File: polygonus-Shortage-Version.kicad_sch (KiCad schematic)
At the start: 10 parts, among them J1 Conn_01x01, J2 Conn_01x01, J3 Conn_01x01, J4 Conn_01x32, J5 Conn_01x32, J6 Conn_01x16, J7 Conn_01x16

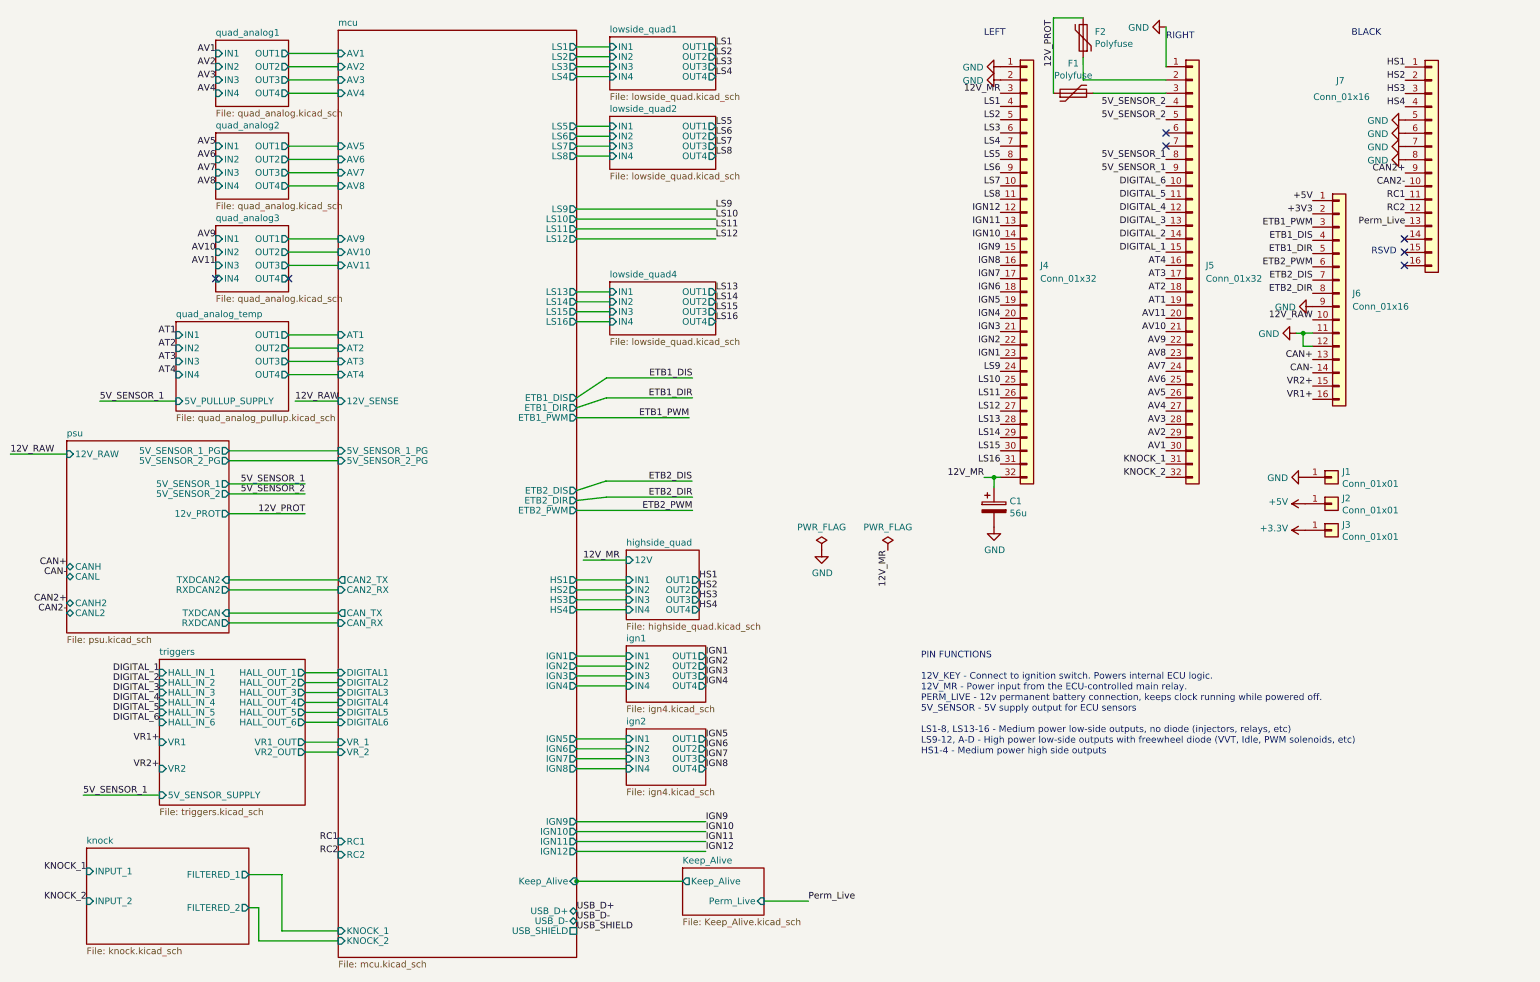
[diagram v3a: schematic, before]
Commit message: route trigger scope
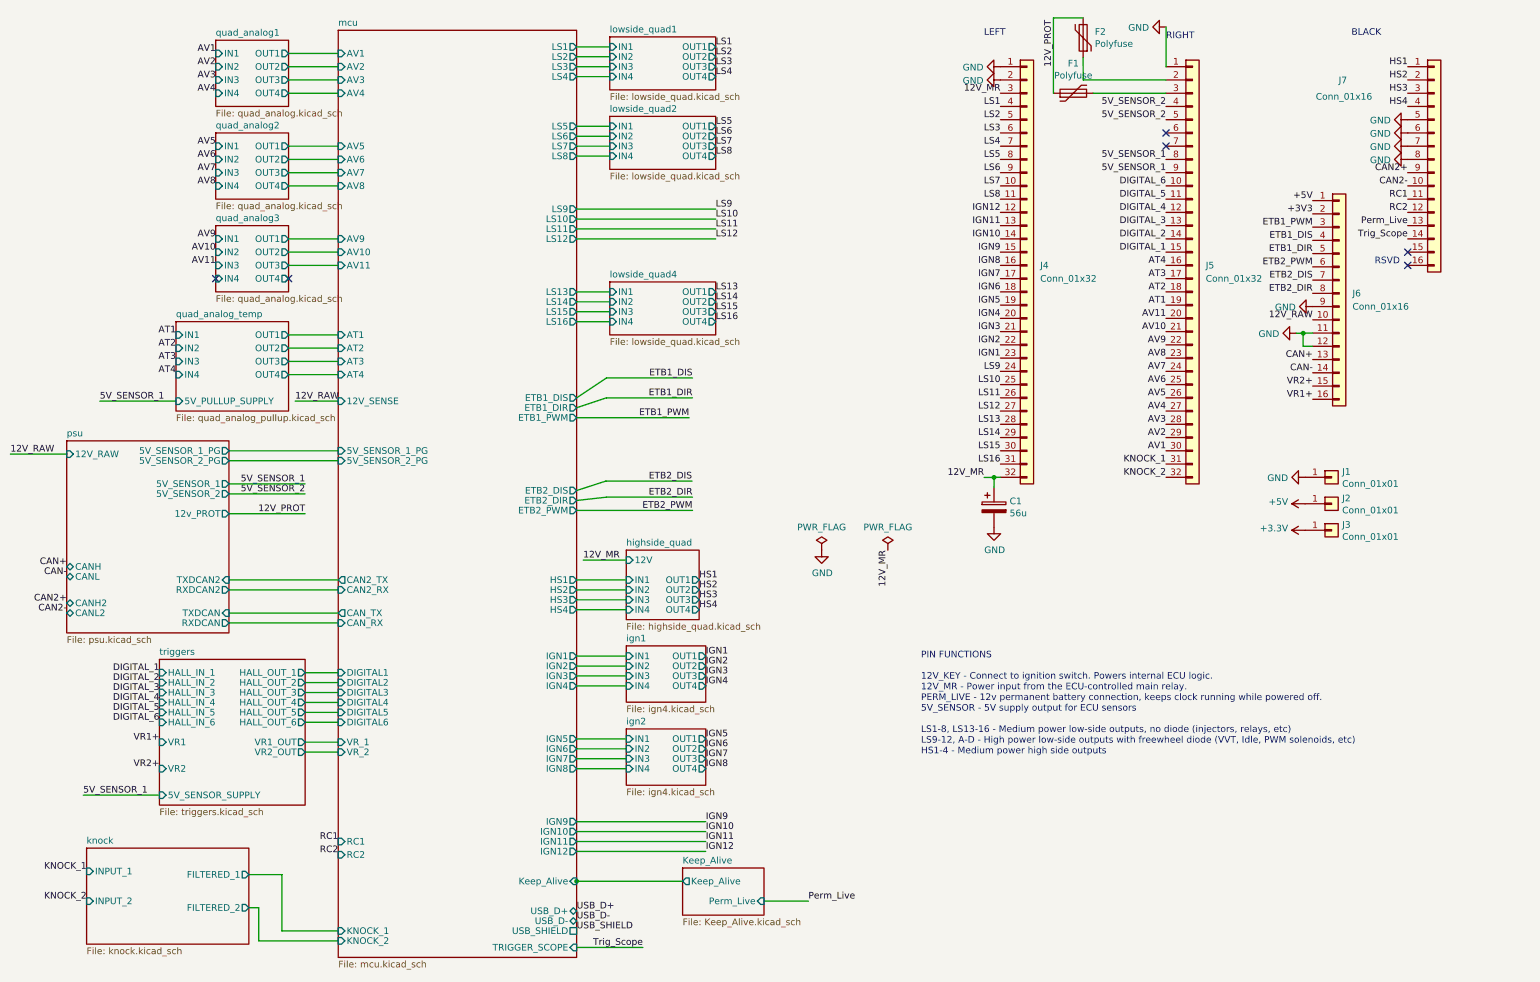
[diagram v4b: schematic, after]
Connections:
- net Trig_Scope: now reaches J7.14 (Pin_14)
- no-connect marks 7 -> 6
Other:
- sheet mcu ports: added TRIGGER_SCOPE; removed none
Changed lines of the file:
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@@
   )
   (no_connect (at 45.085 64.77))
+  (no_connect (at 273.685 59.69))
   (no_connect (at 59.055 64.77))
-  (no_connect (at 273.05 59.69))
   (no_connect (at 227.33 36.83))
   (no_connect (at 227.33 39.37))
-  (no_connect (at 273.05 62.23))
-  (no_connect (at 273.05 57.15))
+  (no_connect (at 273.685 62.23))
   (wire (pts (xy 62.23 144.145) (xy 68.58 144.145))
     (stroke (width 0) (type default))
@@
     (stroke (width 0) (type default))
   )
+  (wire (pts (xy 114.3 193.04) (xy 127 193.04))
+    (stroke (width 0) (type default))
+  )
   (wire (pts (xy 114.3 139.065) (xy 123.825 139.065))
     (stroke (width 0) (type default))
@@
     (effects (font (size 1.27 1.27)) (justify left bottom))
   )
-  (text "RSVD" (at 266.7 60.325 0)
+  (text "RSVD" (at 267.335 62.23 0)
     (effects (font (size 1.27 1.27)) (justify left bottom))
   )
@@
     (effects (font (size 1.27 1.27)) (justify right bottom))
   )
-  (label "HS1" (at 273.2114 24.1919 180) (fields_autoplaced)
-    (effects (font (size 1.27 1.27)) (justify right bottom))
-  )
-  (label "CAN2-" (at 273.2114 47.0519 180) (fields_autoplaced)
+  (label "HS1" (at 273.685 24.13 180) (fields_autoplaced)
+    (effects (font (size 1.27 1.27)) (justify right bottom))
+  )
+  (label "CAN2-" (at 273.685 46.99 180) (fields_autoplaced)
     (effects (font (size 1.27 1.27)) (justify right bottom))
   )
@@
     (effects (font (size 1.27 1.27)) (justify right bottom))
   )
+  (label "Trig_Scope" (at 273.685 57.15 180) (fields_autoplaced)
+    (effects (font (size 1.27 1.27)) (justify right bottom))
+  )
   (label "DIGITAL_3" (at 227.33 54.61 180) (fields_autoplaced)
     (effects (font (size 1.27 1.27)) (justify right bottom))
@@
     (effects (font (size 1.27 1.27)) (justify right bottom))
   )
-  (label "RC2" (at 273.2114 52.1319 180) (fields_autoplaced)
+  (label "RC2" (at 273.685 52.07 180) (fields_autoplaced)
     (effects (font (size 1.27 1.27)) (justify right bottom))
   )
@@
     (effects (font (size 1.27 1.27)) (justify right bottom))
   )
-  (label "HS3" (at 273.2114 29.2719 180) (fields_autoplaced)
+  (label "HS3" (at 273.685 29.21 180) (fields_autoplaced)
     (effects (font (size 1.27 1.27)) (justify right bottom))
   )
@@
     (effects (font (size 1.27 1.27)) (justify right bottom))
   )
-  (label "HS2" (at 273.2114 26.7319 180) (fields_autoplaced)
+  (label "HS2" (at 273.685 26.67 180) (fields_autoplaced)
     (effects (font (size 1.27 1.27)) (justify right bottom))
   )
@@
     (effects (font (size 1.27 1.27)) (justify left bottom))
   )
-  (label "Perm_Live" (at 273.2114 54.6719 180) (fields_autoplaced)
-    (effects (font (size 1.27 1.27)) (justify right bottom))
-  )
-  (label "RC1" (at 273.2114 49.5919 180) (fields_autoplaced)
+  (label "Perm_Live" (at 273.685 54.61 180) (fields_autoplaced)
+    (effects (font (size 1.27 1.27)) (justify right bottom))
+  )
+  (label "RC1" (at 273.685 49.53 180) (fields_autoplaced)
     (effects (font (size 1.27 1.27)) (justify right bottom))
   )
@@
     (effects (font (size 1.27 1.27)) (justify right bottom))
   )
+  (label "Trig_Scope" (at 127 193.04 180) (fields_autoplaced)
+    (effects (font (size 1.27 1.27)) (justify right bottom))
+  )
   (label "AT4" (at 227.33 62.23 180) (fields_autoplaced)
     (effects (font (size 1.27 1.27)) (justify right bottom))
@@
     (effects (font (size 1.27 1.27)) (justify right bottom))
   )
-  (label "CAN2+" (at 273.2114 44.5119 180) (fields_autoplaced)
+  (label "CAN2+" (at 273.685 44.45 180) (fields_autoplaced)
     (effects (font (size 1.27 1.27)) (justify right bottom))
   )
@@
     (effects (font (size 1.27 1.27)) (justify left bottom))
   )
-  (label "HS4" (at 273.2114 31.8119 180) (fields_autoplaced)
+  (label "HS4" (at 273.685 31.75 180) (fields_autoplaced)
     (effects (font (size 1.27 1.27)) (justify right bottom))
   )
@@
     )
   )
-  (symbol (lib_id "power:GND") (at 273.2114 39.4319 270) (unit 1)
-    (in_bom yes) (on_board yes) (dnp no)
-    (property "Reference" "#PWR013" (at 266.8614 39.4319 0)
-      (effects (font (size 1.27 1.27)) hide)
-    )
-    (property "Value" "GND" (at 269.9602 39.5589 90)
-      (effects (font (size 1.27 1.27)) (justify right))
-    )
-    (property "Footprint" "" (at 273.2114 39.4319 0)
-      (effects (font (size 1.27 1.27)) hide)
-    )
-    (property "Datasheet" "" (at 273.2114 39.4319 0)
+  (symbol (lib_id "power:GND") (at 273.685 39.37 270) (unit 1)
+    (in_bom yes) (on_board yes) (dnp no)
+    (property "Reference" "#PWR013" (at 267.335 39.37 0)
+      (effects (font (size 1.27 1.27)) hide)
+    )
+    (property "Value" "GND" (at 270.4338 39.497 90)
+      (effects (font (size 1.27 1.27)) (justify right))
+    )
+    (property "Footprint" "" (at 273.685 39.37 0)
+      (effects (font (size 1.27 1.27)) hide)
+    )
+    (property "Datasheet" "" (at 273.685 39.37 0)
       (effects (font (size 1.27 1.27)) hide)
     )
@@
     )
   )
-  (symbol (lib_id "power:GND") (at 273.2114 41.9719 270) (unit 1)
-    (in_bom yes) (on_board yes) (dnp no)
-    (property "Reference" "#PWR014" (at 266.8614 41.9719 0)
-      (effects (font (size 1.27 1.27)) hide)
-    )
-    (property "Value" "GND" (at 269.9602 42.0989 90)
-      (effects (font (size 1.27 1.27)) (justify right))
-    )
-    (property "Footprint" "" (at 273.2114 41.9719 0)
-      (effects (font (size 1.27 1.27)) hide)
-    )
-    (property "Datasheet" "" (at 273.2114 41.9719 0)
+  (symbol (lib_id "power:GND") (at 273.685 41.91 270) (unit 1)
+    (in_bom yes) (on_board yes) (dnp no)
+    (property "Reference" "#PWR014" (at 267.335 41.91 0)
+      (effects (font (size 1.27 1.27)) hide)
+    )
+    (property "Value" "GND" (at 270.4338 42.037 90)
+      (effects (font (size 1.27 1.27)) (justify right))
+    )
+    (property "Footprint" "" (at 273.685 41.91 0)
+      (effects (font (size 1.27 1.27)) hide)
+    )
+    (property "Datasheet" "" (at 273.685 41.91 0)
       (effects (font (size 1.27 1.27)) hide)
     )
@@
     )
   )
-  (symbol (lib_id "power:GND") (at 273.2114 34.3519 270) (unit 1)
-    (in_bom yes) (on_board yes) (dnp no)
-    (property "Reference" "#PWR011" (at 266.8614 34.3519 0)
-      (effects (font (size 1.27 1.27)) hide)
-    )
-    (property "Value" "GND" (at 269.9602 34.4789 90)
-      (effects (font (size 1.27 1.27)) (justify right))
-    )
-    (property "Footprint" "" (at 273.2114 34.3519 0)
-      (effects (font (size 1.27 1.27)) hide)
-    )
-    (property "Datasheet" "" (at 273.2114 34.3519 0)
+  (symbol (lib_id "power:GND") (at 273.685 34.29 270) (unit 1)
+    (in_bom yes) (on_board yes) (dnp no)
+    (property "Reference" "#PWR011" (at 267.335 34.29 0)
+      (effects (font (size 1.27 1.27)) hide)
+    )
+    (property "Value" "GND" (at 270.4338 34.417 90)
+      (effects (font (size 1.27 1.27)) (justify right))
+    )
+    (property "Footprint" "" (at 273.685 34.29 0)
+      (effects (font (size 1.27 1.27)) hide)
+    )
+    (property "Datasheet" "" (at 273.685 34.29 0)
       (effects (font (size 1.27 1.27)) hide)
     )
@@
     )
   )
-  (symbol (lib_id "power:GND") (at 273.2114 36.8919 270) (unit 1)
-    (in_bom yes) (on_board yes) (dnp no)
-    (property "Reference" "#PWR012" (at 266.8614 36.8919 0)
-      (effects (font (size 1.27 1.27)) hide)
-    )
-    (property "Value" "GND" (at 269.9602 37.0189 90)
-      (effects (font (size 1.27 1.27)) (justify right))
-    )
-    (property "Footprint" "" (at 273.2114 36.8919 0)
-      (effects (font (size 1.27 1.27)) hide)
-    )
-    (property "Datasheet" "" (at 273.2114 36.8919 0)
+  (symbol (lib_id "power:GND") (at 273.685 36.83 270) (unit 1)
+    (in_bom yes) (on_board yes) (dnp no)
+    (property "Reference" "#PWR012" (at 267.335 36.83 0)
+      (effects (font (size 1.27 1.27)) hide)
+    )
+    (property "Value" "GND" (at 270.4338 36.957 90)
+      (effects (font (size 1.27 1.27)) (justify right))
+    )
+    (property "Footprint" "" (at 273.685 36.83 0)
+      (effects (font (size 1.27 1.27)) hide)
+    )
+    (property "Datasheet" "" (at 273.685 36.83 0)
       (effects (font (size 1.27 1.27)) hide)
     )
@@
     )
   )
-  (symbol (lib_id "Connector_Generic:Conn_01x16") (at 278.2914 41.9719 0) (unit 1)
-    (in_bom yes) (on_board yes) (dnp no)
-    (property "Reference" "J7" (at 259.9581 26.7811 0)
-      (effects (font (size 1.27 1.27)) (justify left))
-    )
-    (property "Value" "Conn_01x16" (at 255.5749 29.9238 0)
-      (effects (font (size 1.27 1.27)) (justify left))
-    )
-    (property "Footprint" "Connector_PinHeader_2.54mm:PinHeader_1x16_P2.54mm_Vertical" (at 278.2914 41.9719 0)
-      (effects (font (size 1.27 1.27)) hide)
-    )
-    (property "Datasheet" "~" (at 278.2914 41.9719 0)
+  (symbol (lib_id "Connector_Generic:Conn_01x16") (at 278.765 41.91 0) (unit 1)
+    (in_bom yes) (on_board yes) (dnp no)
+    (property "Reference" "J7" (at 260.4317 26.7192 0)
+      (effects (font (size 1.27 1.27)) (justify left))
+    )
+    (property "Value" "Conn_01x16" (at 256.0485 29.8619 0)
+      (effects (font (size 1.27 1.27)) (justify left))
+    )
+    (property "Footprint" "Connector_PinHeader_2.54mm:PinHeader_1x16_P2.54mm_Vertical" (at 278.765 41.91 0)
+      (effects (font (size 1.27 1.27)) hide)
+    )
+    (property "Datasheet" "~" (at 278.765 41.91 0)
       (effects (font (size 1.27 1.27)) hide)
     )
@@
       (effects (font (size 1.27 1.27)) (justify left))
     )
-    (instances
+    (pin "TRIGGER_SCOPE" input (at 114.3 193.04 0)
+      (effects (font (size 1.27 1.27)) (justify right))
+    )
+    (instances
